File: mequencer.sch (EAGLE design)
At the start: 62 parts, among them IC1 NE555D, IC10 LF353D, IC11 NE555D, IC12 NE555D, IC2 4163D, IC3 74HC85D, IC4 4051D, IC5 4051D, IC6 74HCT04D, IC7 4051D, IC8 4051D, IC9 LF353D, U1 74LVC1G08SE-7

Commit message: mini boards
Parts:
- added FRAME2: FRAME-LETTER, SparkFun-Aesthetics:FRAME-LETTER
- added JP10, JP11, JP12, JP13, JP14, JP15, JP16, JP17, JP4, JP5, JP6, JP7, JP8, JP9: (no value), SparkFun-Connectors:M04JST-PTH
- added U$7: M08X2, SparkFun-Connectors:M08X2
- JP2, JP3: value M20 -> (none); device SparkFun-Connectors:M20 -> SparkFun-Connectors:M04JST-PTH
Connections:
- removed net CANNEL3: JP2.4
- removed net N$29: JP3.19
- new net VCC: JP10.4, JP11.4, JP12.4, JP13.4, JP14.4, JP15.4, JP16.4, JP17.4, JP2.4, JP3.4, JP4.4, JP5.4, JP6.4, JP7.4, JP8.4, JP9.4
- net 5V: now also U$7.1; no longer JP3.20
- net CHANNEL0: no longer JP2.1
- net CHANNEL1: no longer JP2.2
- net CHANNEL10: no longer JP2.11
- net CHANNEL11: no longer JP2.12
- net CHANNEL12: no longer JP2.13
- net CHANNEL13: no longer JP2.14
- net CHANNEL14: no longer JP2.15
- net CHANNEL15: no longer JP2.16
- net CHANNEL2: no longer JP2.3
- net CHANNEL4: no longer JP2.5
- net CHANNEL5: no longer JP2.6
- net CHANNEL6: no longer JP2.7
- net CHANNEL7: no longer JP2.8
- net CHANNEL8: no longer JP2.9
- net CHANNEL9: no longer JP2.10
- net CLOCK_SPEED: now also U$7.7; no longer JP2.17
- net GND: now also JP10.1, JP11.1, JP12.1, JP13.1, JP14.1, JP15.1, JP16.1, JP17.1, JP2.1, JP3.1, JP4.1, JP5.1, JP6.1, JP7.1, JP8.1, JP9.1, U$7.16; no longer JP2.20
- net LED0: now also JP2.3; no longer JP3.1
- net LED1: now also JP3.3; no longer JP3.2
- net LED10: now also JP12.3; no longer JP3.11
- net LED11: now also JP13.3; no longer JP3.12
- net LED12: now also JP14.3; no longer JP3.13
- net LED13: now also JP15.3; no longer JP3.14
- net LED14: now also JP16.3; no longer JP3.15
- net LED15: now also JP17.3; no longer JP3.16
- net LED2: now also JP4.3; no longer JP3.3
- net LED3: now also JP5.3; no longer JP3.4
- net LED4: now also JP6.3; no longer JP3.5
- net LED5: now also JP7.3; no longer JP3.6
- net LED6: now also JP8.3; no longer JP3.7
- net LED7: now also JP9.3; no longer JP3.8
- net LED8: now also JP10.3; no longer JP3.9
- net LED9: now also JP11.3; no longer JP3.10
- net LOAD: now also U$7.11; no longer JP3.17
- net LOAD0: now also U$7.6
- net LOAD1: now also U$7.8
- net LOAD2: now also U$7.10
- net LOAD3: now also U$7.12
- net N$16: now also U$7.14
- net NOTE_LENGTH: now also U$7.9; no longer JP3.18
- net PAUSE_IN: now also U$7.3; no longer JP2.18
- net PAUSE_OUT: now also U$7.5; no longer JP2.19
- net RESET0: now also U$7.13
- net RESET1: now also U$7.15
- net RESET2: now also U$7.2
- net RESET3: now also U$7.4

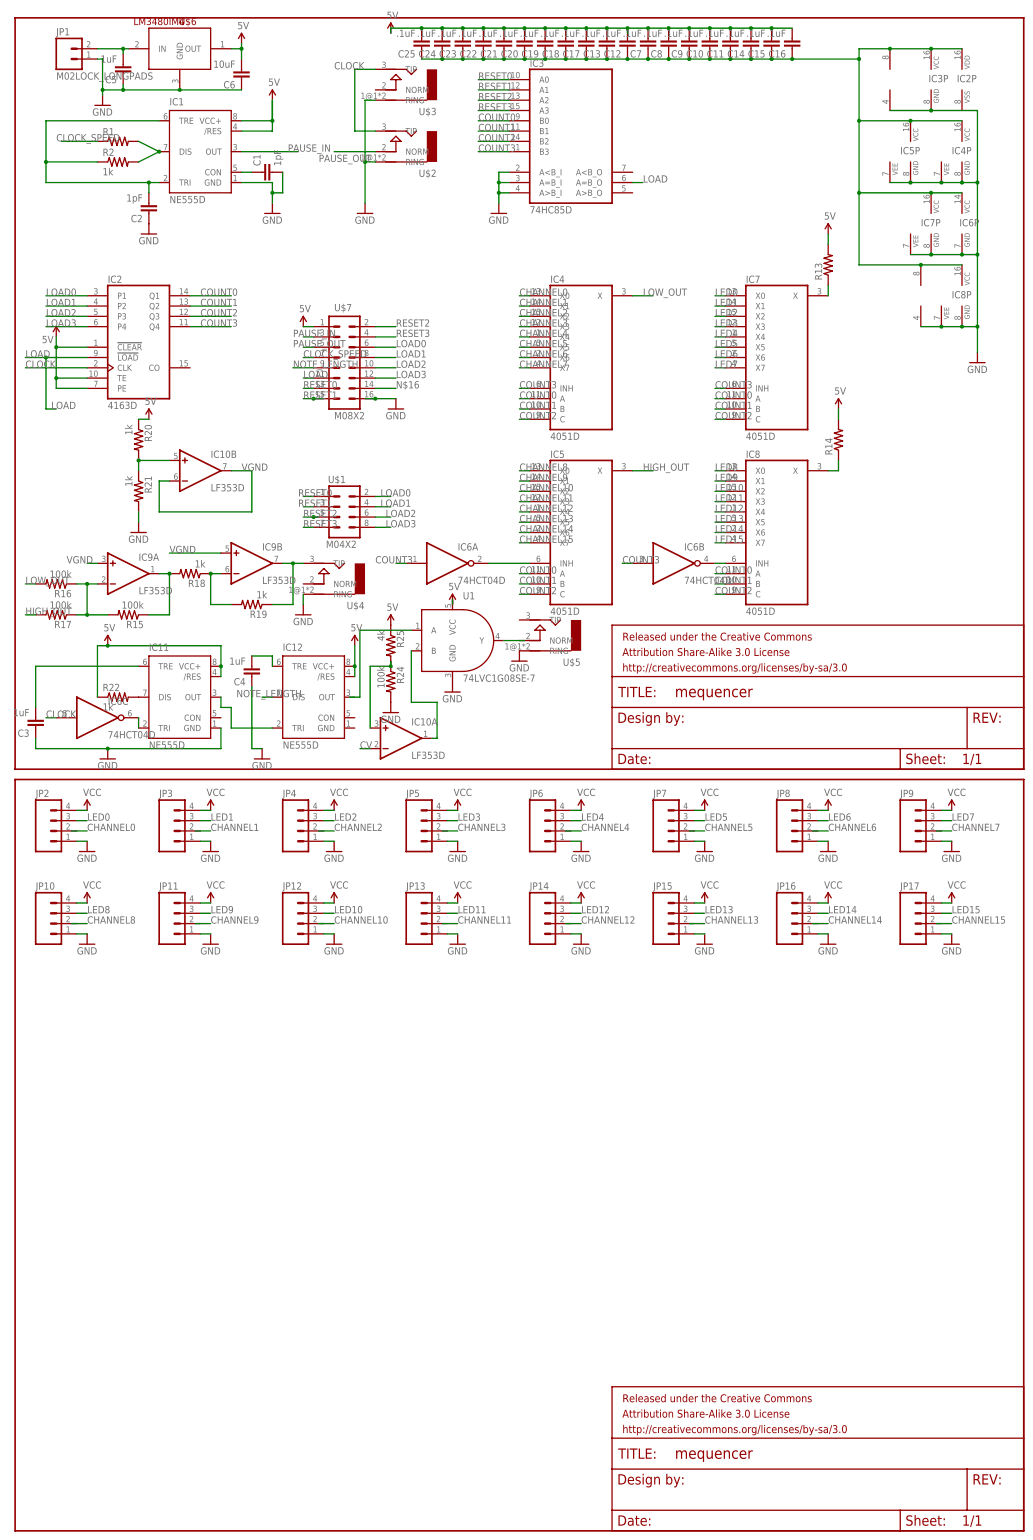
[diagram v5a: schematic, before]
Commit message: Knobby board layed out with 4 jacks
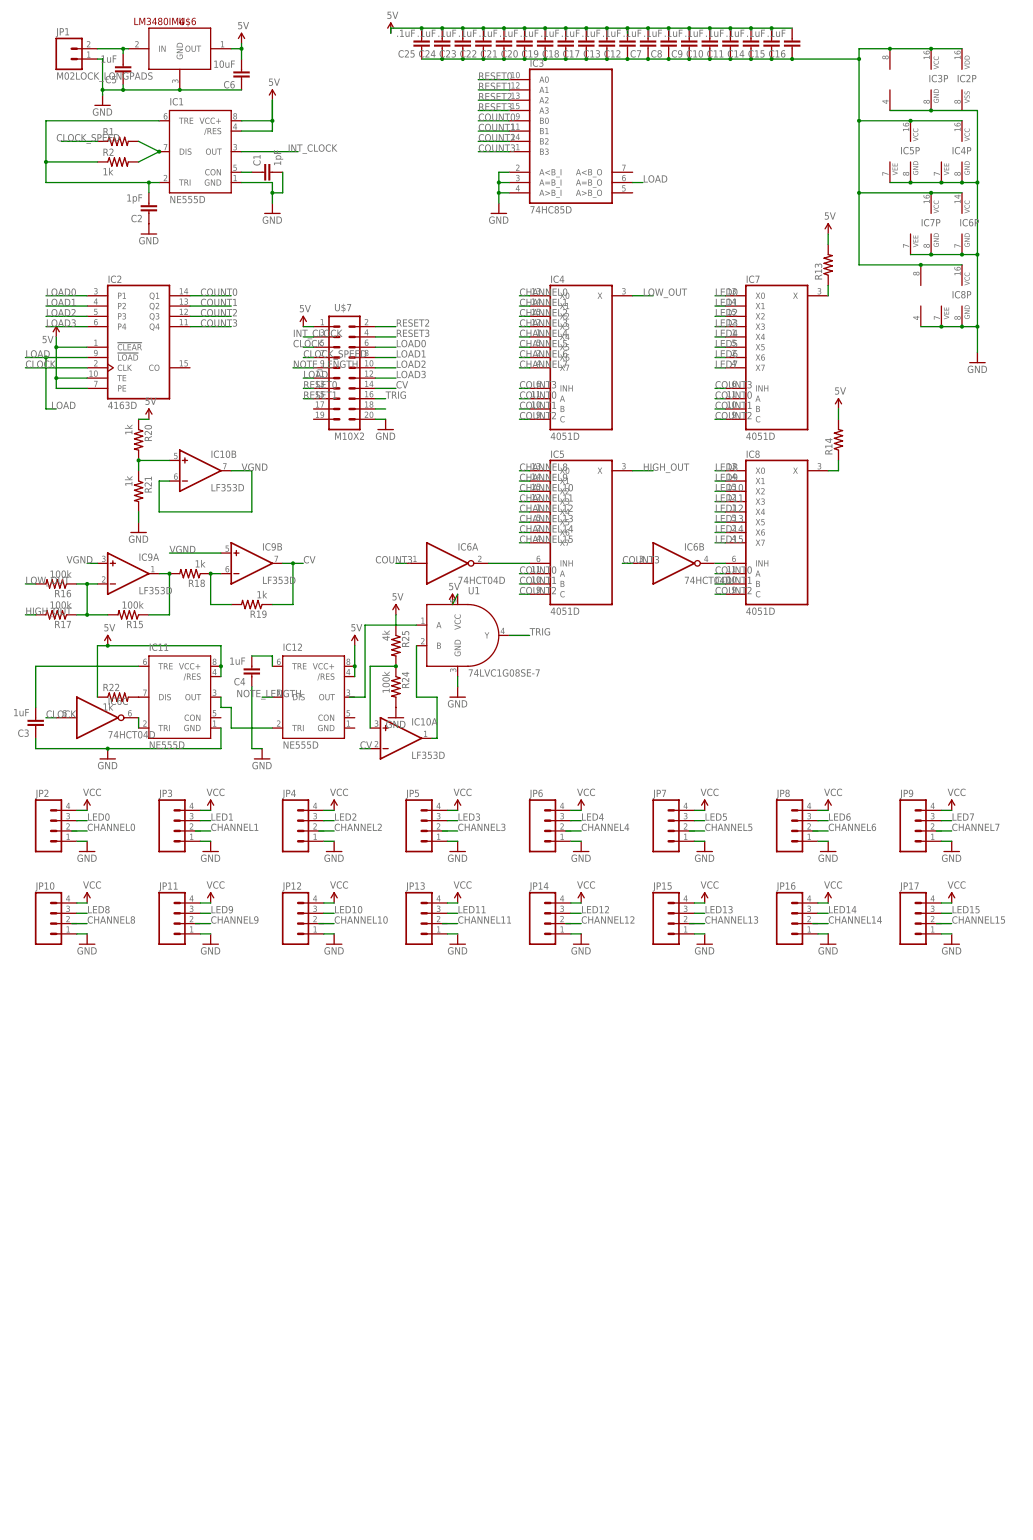
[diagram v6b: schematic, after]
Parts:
- removed FRAME1, FRAME2: FRAME-LETTER, SparkFun-Aesthetics:FRAME-LETTER
- removed U$1: M04X2, SparkFun-Connectors:M04X2
- removed U$2, U$3, U$4, U$5: AUDIO-JACKERTHENVAR, erthenvar:AUDIO-JACKERTHENVAR
- U$7: value M08X2 -> M10X2; device SparkFun-Connectors:M08X2 -> SparkFun-Connectors:M10X2
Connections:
- net PAUSE_IN renamed INT_CLOCK
- removed net N$14: IC9B.OUT, R19.1, U$4.TIP
- removed net N$26: U1.Y
- removed net PAUSE_OUT: U$2.NORM, U$7.5
- new net N$6: U$7.18
- new net TRIG: U$7.16, U1.Y
- net CLOCK: now also U$7.5; no longer U$2.TIP, U$3.TIP
- net CV: now also IC9B.OUT, R19.1, U$7.14
- net GND: now also U$7.20; no longer U$2.RING, U$3.RING, U$4.RING, U$5.RING, U$7.16
- net LOAD0: no longer U$1.2
- net LOAD1: no longer U$1.4
- net LOAD2: no longer U$1.6
- net LOAD3: no longer U$1.8
- net N$16: no longer U$7.14
- net RESET0: no longer U$1.1
- net RESET1: no longer U$1.3
- net RESET2: no longer U$1.5
- net RESET3: no longer U$1.7
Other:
- moved on the sheet: R24, R25, U1

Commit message: through hole led on mini boards
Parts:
- removed U$7: M10X2, SparkFun-Connectors:M10X2
- added STANDOFF1, STANDOFF2, STANDOFF3, STANDOFF4: STAND-OFF, SparkFun-Electromechanical:STAND-OFF
- added U$2: M10X2, SparkFun-Connectors:M10X2
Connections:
- removed net N$6: U$7.18
- net 5V: now also U$2.1; no longer U$7.1
- net CLOCK: now also U$2.5; no longer U$7.5
- net CLOCK_SPEED: now also U$2.7; no longer U$7.7
- net CV: now also U$2.17; no longer U$7.14
- net GND: now also U$2.20; no longer U$7.20
- net INT_CLOCK: now also U$2.3; no longer U$7.3
- net LOAD: now also U$2.11; no longer U$7.11
- net LOAD0: now also U$2.8; no longer U$7.6
- net LOAD1: now also U$2.6; no longer U$7.8
- net LOAD2: now also U$2.4; no longer U$7.10
- net LOAD3: now also U$2.2; no longer U$7.12
- net NOTE_LENGTH: now also U$2.9; no longer U$7.9
- net RESET0: now also U$2.16; no longer U$7.13
- net RESET1: now also U$2.14; no longer U$7.15
- net RESET2: now also U$2.12; no longer U$7.2
- net RESET3: now also U$2.10; no longer U$7.4
- net TRIG: now also U$2.19; no longer U$7.16
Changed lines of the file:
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@@
 <part name="C25" library="SparkFun-Capacitors" deviceset="CAP" device="0603-CAP" value=".1uF"/>
 <part name="R2" library="SparkFun-Resistors" deviceset="RESISTOR" device="0603" value="1k"/>
-<part name="U$7" library="SparkFun-Connectors" deviceset="M10X2" device=""/>
-<part name="SUPPLY4" library="SparkFun-Aesthetics" deviceset="5V" device=""/>
-<part name="GND5" library="SparkFun-Aesthetics" deviceset="GND" device=""/>
 <part name="JP2" library="SparkFun-Connectors" deviceset="M04" device="JST-PTH"/>
 <part name="SUPPLY1" library="SparkFun-Aesthetics" deviceset="VCC" device=""/>
@@
 <part name="SUPPLY28" library="SparkFun-Aesthetics" deviceset="VCC" device=""/>
 <part name="GND30" library="SparkFun-Aesthetics" deviceset="GND" device=""/>
+<part name="STANDOFF1" library="SparkFun-Electromechanical" deviceset="STAND-OFF" device=""/>
+<part name="STANDOFF2" library="SparkFun-Electromechanical" deviceset="STAND-OFF" device=""/>
+<part name="STANDOFF3" library="SparkFun-Electromechanical" deviceset="STAND-OFF" device=""/>
+<part name="STANDOFF4" library="SparkFun-Electromechanical" deviceset="STAND-OFF" device=""/>
+<part name="U$2" library="SparkFun-Connectors" deviceset="M10X2" device=""/>
+<part name="SUPPLY29" library="SparkFun-Aesthetics" deviceset="5V" device=""/>
+<part name="GND3" library="SparkFun-Aesthetics" deviceset="GND" device=""/>
 </parts>
 <sheets>
@@
 <instance part="C25" gate="G$1" x="100.33" y="180.34" rot="R180"/>
 <instance part="R2" gate="G$1" x="25.4" y="149.86"/>
-<instance part="U$7" gate="G$1" x="81.28" y="99.06"/>
-<instance part="SUPPLY4" gate="G$1" x="71.12" y="109.22"/>
-<instance part="GND5" gate="1" x="91.44" y="83.82"/>
 <instance part="JP2" gate="G$1" x="10.16" y="-15.24"/>
 <instance part="SUPPLY1" gate="1" x="17.78" y="-10.16"/>
@@
 <instance part="SUPPLY28" gate="1" x="231.14" y="-33.02"/>
 <instance part="GND30" gate="1" x="231.14" y="-43.18"/>
+<instance part="STANDOFF1" gate="G$1" x="139.7" y="10.16"/>
+<instance part="STANDOFF2" gate="G$1" x="147.32" y="10.16"/>
+<instance part="STANDOFF3" gate="G$1" x="154.94" y="10.16"/>
+<instance part="STANDOFF4" gate="G$1" x="162.56" y="10.16"/>
+<instance part="U$2" gate="G$1" x="88.9" y="104.14"/>
+<instance part="SUPPLY29" gate="G$1" x="78.74" y="114.3"/>
+<instance part="GND3" gate="1" x="101.6" y="88.9"/>
 </instances>
 <busses>
@@
 </segment>
 <segment>
-<pinref part="U$7" gate="G$1" pin="1"/>
-<wire x1="73.66" y1="109.22" x2="71.12" y2="109.22" width="0.1524" layer="91"/>
-<pinref part="SUPPLY4" gate="G$1" pin="5V"/>
+<pinref part="U$2" gate="G$1" pin="1"/>
+<wire x1="81.28" y1="114.3" x2="78.74" y2="114.3" width="0.1524" layer="91"/>
+<pinref part="SUPPLY29" gate="G$1" pin="5V"/>
 </segment>
 </net>
@@
 </segment>
 <segment>
-<pinref part="U$7" gate="G$1" pin="20"/>
-<wire x1="88.9" y1="86.36" x2="91.44" y2="86.36" width="0.1524" layer="91"/>
-<pinref part="GND5" gate="1" pin="GND"/>
+<pinref part="GND3" gate="1" pin="GND"/>
+<pinref part="U$2" gate="G$1" pin="20"/>
+<wire x1="101.6" y1="91.44" x2="96.52" y2="91.44" width="0.1524" layer="91"/>
 </segment>
 </net>
@@
 </segment>
 <segment>
-<pinref part="U$7" gate="G$1" pin="5"/>
-<wire x1="73.66" y1="104.14" x2="71.12" y2="104.14" width="0.1524" layer="91"/>
-<label x="68.58" y="104.14" size="1.778" layer="95"/>
+<pinref part="U$2" gate="G$1" pin="5"/>
+<wire x1="81.28" y1="109.22" x2="78.74" y2="109.22" width="0.1524" layer="91"/>
+<label x="78.74" y="109.22" size="1.778" layer="95"/>
 </segment>
 </net>
@@
 </segment>
 <segment>
-<pinref part="U$7" gate="G$1" pin="11"/>
-<wire x1="73.66" y1="96.52" x2="71.12" y2="96.52" width="0.1524" layer="91"/>
-<label x="71.12" y="96.52" size="1.778" layer="95"/>
+<pinref part="U$2" gate="G$1" pin="11"/>
+<wire x1="81.28" y1="101.6" x2="78.74" y2="101.6" width="0.1524" layer="91"/>
+<label x="78.74" y="101.6" size="1.778" layer="95"/>
 </segment>
 </net>
@@
 </segment>
 <segment>
-<pinref part="U$7" gate="G$1" pin="6"/>
-<wire x1="88.9" y1="104.14" x2="93.98" y2="104.14" width="0.1524" layer="91"/>
-<label x="93.98" y="104.14" size="1.778" layer="95"/>
+<pinref part="U$2" gate="G$1" pin="8"/>
+<wire x1="96.52" y1="106.68" x2="101.6" y2="106.68" width="0.1524" layer="91"/>
+<label x="101.6" y="106.68" size="1.778" layer="95"/>
 </segment>
 </net>
@@
 </segment>
 <segment>
-<pinref part="U$7" gate="G$1" pin="8"/>
-<wire x1="88.9" y1="101.6" x2="93.98" y2="101.6" width="0.1524" layer="91"/>
-<label x="93.98" y="101.6" size="1.778" layer="95"/>
+<pinref part="U$2" gate="G$1" pin="6"/>
+<wire x1="96.52" y1="109.22" x2="101.6" y2="109.22" width="0.1524" layer="91"/>
+<label x="101.6" y="109.22" size="1.778" layer="95"/>
 </segment>
 </net>
@@
 </segment>
 <segment>
-<pinref part="U$7" gate="G$1" pin="10"/>
-<wire x1="88.9" y1="99.06" x2="93.98" y2="99.06" width="0.1524" layer="91"/>
-<label x="93.98" y="99.06" size="1.778" layer="95"/>
+<pinref part="U$2" gate="G$1" pin="4"/>
+<wire x1="96.52" y1="111.76" x2="101.6" y2="111.76" width="0.1524" layer="91"/>
+<label x="101.6" y="111.76" size="1.778" layer="95"/>
 </segment>
 </net>
@@
 </segment>
 <segment>
-<pinref part="U$7" gate="G$1" pin="12"/>
-<wire x1="88.9" y1="96.52" x2="93.98" y2="96.52" width="0.1524" layer="91"/>
-<label x="93.98" y="96.52" size="1.778" layer="95"/>
+<pinref part="U$2" gate="G$1" pin="2"/>
+<wire x1="96.52" y1="114.3" x2="101.6" y2="114.3" width="0.1524" layer="91"/>
+<label x="101.6" y="114.3" size="1.778" layer="95"/>
 </segment>
 </net>
@@
 </segment>
 <segment>
-<pinref part="U$7" gate="G$1" pin="13"/>
-<wire x1="73.66" y1="93.98" x2="71.12" y2="93.98" width="0.1524" layer="91"/>
-<label x="71.12" y="93.98" size="1.778" layer="95"/>
+<pinref part="U$2" gate="G$1" pin="16"/>
+<wire x1="96.52" y1="96.52" x2="101.6" y2="96.52" width="0.1524" layer="91"/>
+<label x="101.6" y="96.52" size="1.778" layer="95"/>
 </segment>
 </net>
@@
 </segment>
 <segment>
-<label x="71.12" y="91.44" size="1.778" layer="95"/>
-<pinref part="U$7" gate="G$1" pin="15"/>
-<wire x1="73.66" y1="91.44" x2="71.12" y2="91.44" width="0.1524" layer="91"/>
+<pinref part="U$2" gate="G$1" pin="14"/>
+<wire x1="96.52" y1="99.06" x2="101.6" y2="99.06" width="0.1524" layer="91"/>
+<label x="101.6" y="99.06" size="1.778" layer="95"/>
 </segment>
 </net>
@@
 </segment>
 <segment>
-<pinref part="U$7" gate="G$1" pin="2"/>
-<wire x1="88.9" y1="109.22" x2="93.98" y2="109.22" width="0.1524" layer="91"/>
-<label x="93.98" y="109.22" size="1.778" layer="95"/>
+<pinref part="U$2" gate="G$1" pin="12"/>
+<wire x1="96.52" y1="101.6" x2="101.6" y2="101.6" width="0.1524" layer="91"/>
+<label x="101.6" y="101.6" size="1.778" layer="95"/>
 </segment>
 </net>
@@
 </segment>
 <segment>
-<pinref part="U$7" gate="G$1" pin="4"/>
-<wire x1="88.9" y1="106.68" x2="93.98" y2="106.68" width="0.1524" layer="91"/>
-<label x="93.98" y="106.68" size="1.778" layer="95"/>
+<pinref part="U$2" gate="G$1" pin="10"/>
+<wire x1="96.52" y1="104.14" x2="101.6" y2="104.14" width="0.1524" layer="91"/>
+<label x="101.6" y="104.14" size="1.778" layer="95"/>
 </segment>
 </net>
@@
 </segment>
 <segment>
-<pinref part="U$7" gate="G$1" pin="14"/>
-<wire x1="88.9" y1="93.98" x2="93.98" y2="93.98" width="0.1524" layer="91"/>
-<label x="93.98" y="93.98" size="1.778" layer="95"/>
-</segment>
-<segment>
 <pinref part="R19" gate="G$1" pin="1"/>
 <wire x1="63.5" y1="40.64" x2="68.58" y2="40.64" width="0.1524" layer="91"/>
@@
 <label x="71.12" y="50.8" size="1.778" layer="95"/>
 </segment>
+<segment>
+<pinref part="U$2" gate="G$1" pin="17"/>
+<wire x1="81.28" y1="93.98" x2="78.74" y2="93.98" width="0.1524" layer="91"/>
+<label x="78.74" y="93.98" size="1.778" layer="95"/>
+</segment>
 </net>
 <net name="N$25" class="0">
@@
 </segment>
 <segment>
-<pinref part="U$7" gate="G$1" pin="7"/>
-<wire x1="73.66" y1="101.6" x2="71.12" y2="101.6" width="0.1524" layer="91"/>
-<label x="71.12" y="101.6" size="1.778" layer="95"/>
+<pinref part="U$2" gate="G$1" pin="7"/>
+<wire x1="81.28" y1="106.68" x2="78.74" y2="106.68" width="0.1524" layer="91"/>
+<label x="78.74" y="106.68" size="1.778" layer="95"/>
 </segment>
 </net>
@@
 </segment>
 <segment>
-<pinref part="U$7" gate="G$1" pin="9"/>
-<wire x1="73.66" y1="99.06" x2="68.58" y2="99.06" width="0.1524" layer="91"/>
-<label x="68.58" y="99.06" size="1.778" layer="95"/>
+<pinref part="U$2" gate="G$1" pin="9"/>
+<wire x1="81.28" y1="104.14" x2="78.74" y2="104.14" width="0.1524" layer="91"/>
+<label x="78.74" y="104.14" size="1.778" layer="95"/>
 </segment>
 </net>
@@
 </segment>
 <segment>
-<pinref part="U$7" gate="G$1" pin="3"/>
-<wire x1="73.66" y1="106.68" x2="71.12" y2="106.68" width="0.1524" layer="91"/>
-<label x="68.58" y="106.68" size="1.778" layer="95"/>
+<pinref part="U$2" gate="G$1" pin="3"/>
+<wire x1="81.28" y1="111.76" x2="78.74" y2="111.76" width="0.1524" layer="91"/>
+<label x="78.74" y="111.76" size="1.778" layer="95"/>
 </segment>
 </net>
 <net name="TRIG" class="0">
-<segment>
-<pinref part="U$7" gate="G$1" pin="16"/>
-<wire x1="88.9" y1="91.44" x2="91.44" y2="91.44" width="0.1524" layer="91"/>
-<label x="91.44" y="91.44" size="1.778" layer="95"/>
-</segment>
 <segment>
 <pinref part="U1" gate="G$1" pin="Y"/>
@@
 <label x="127" y="33.02" size="1.778" layer="95"/>
 </segment>
-</net>
-<net name="N$6" class="0">
-<segment>
-<pinref part="U$7" gate="G$1" pin="18"/>
-<wire x1="88.9" y1="88.9" x2="91.44" y2="88.9" width="0.1524" layer="91"/>
-</segment>
-</net>
+<segment>
+<pinref part="U$2" gate="G$1" pin="19"/>
+<wire x1="81.28" y1="91.44" x2="78.74" y2="91.44" width="0.1524" layer="91"/>
+<label x="78.74" y="91.44" size="1.778" layer="95"/>
+</segment>
+</net>

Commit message: Moving shit around
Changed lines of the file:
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@@
 <segment>
 <pinref part="SUPPLY2" gate="G$1" pin="5V"/>
-<wire x1="63.5" y1="165.1" x2="63.5" y2="160.02" width="0.1524" layer="91"/>
 <pinref part="IC1" gate="G$1" pin="VCC+"/>
 <wire x1="63.5" y1="160.02" x2="55.88" y2="160.02" width="0.1524" layer="91"/>
